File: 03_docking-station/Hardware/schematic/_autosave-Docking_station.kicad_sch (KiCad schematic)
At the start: 22 parts, among them J3 -, J4 +, J5 Conn_01x01, J6 Conn_01x01, J9 Conn_01x02, K1 FINDER-32.21-x000, K2 Relpol, K3 FINDER-32.21-x000, Q1 BC337, U4 LM393

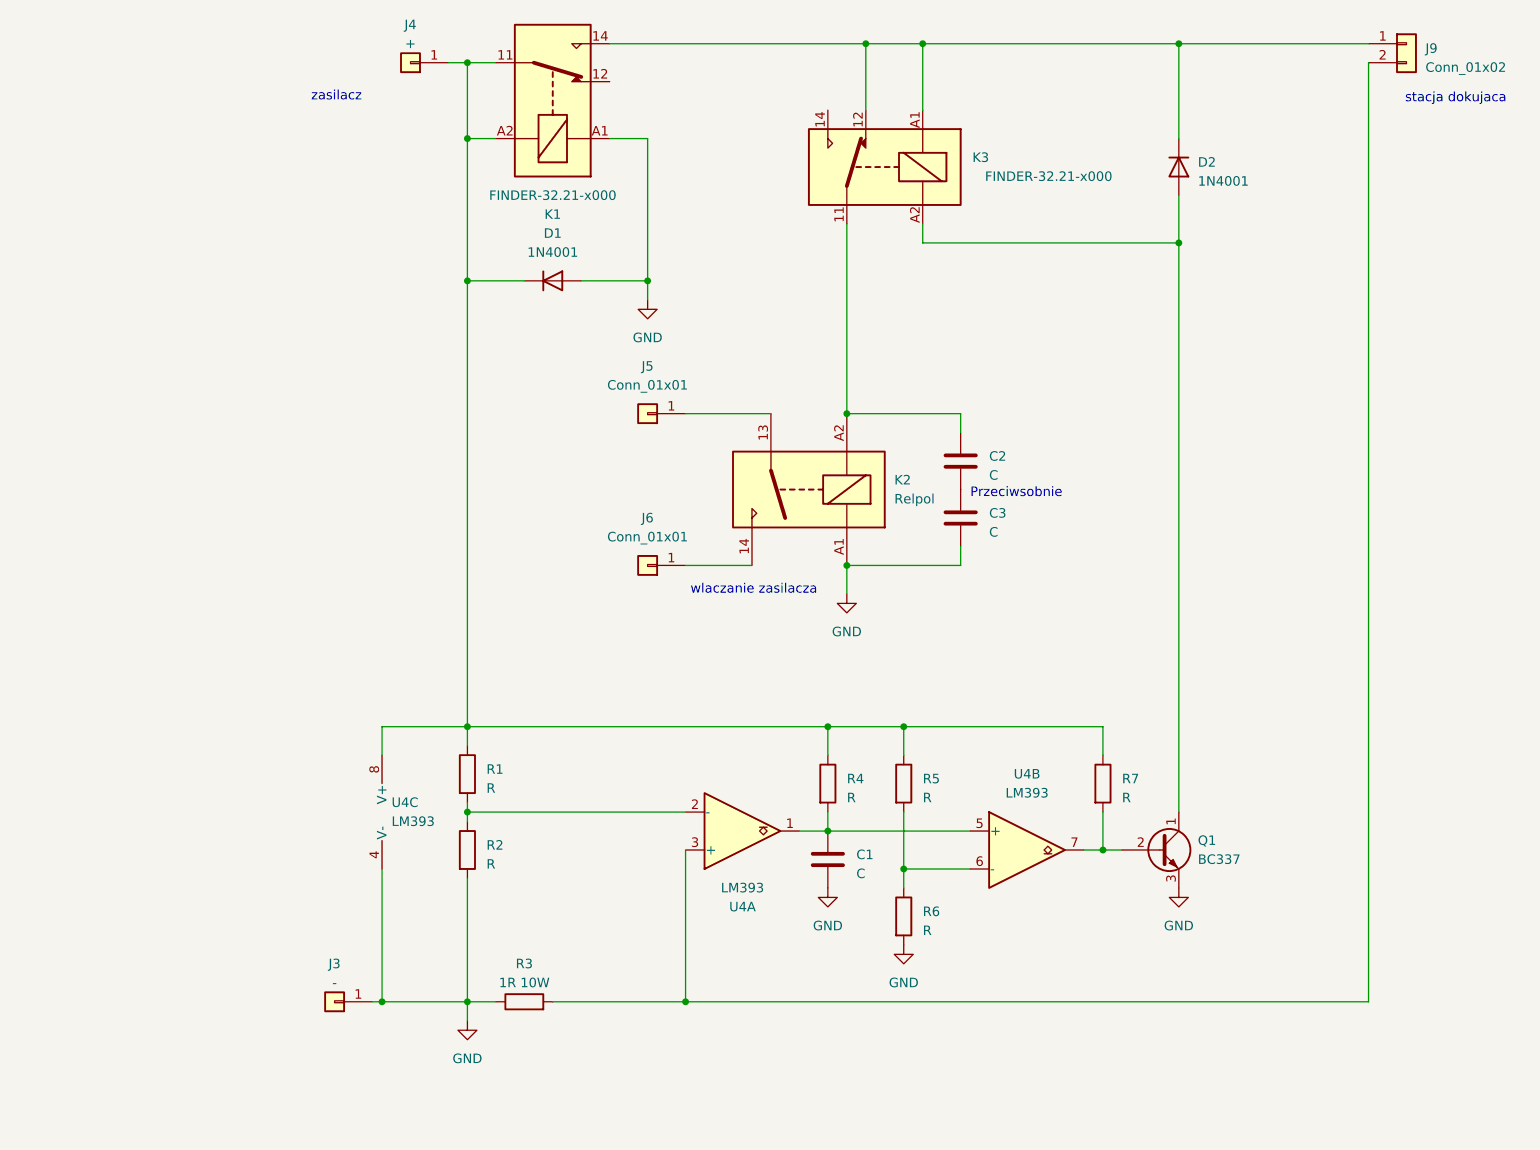
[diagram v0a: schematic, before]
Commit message: minor mistakes fixed; reflected hardware updates
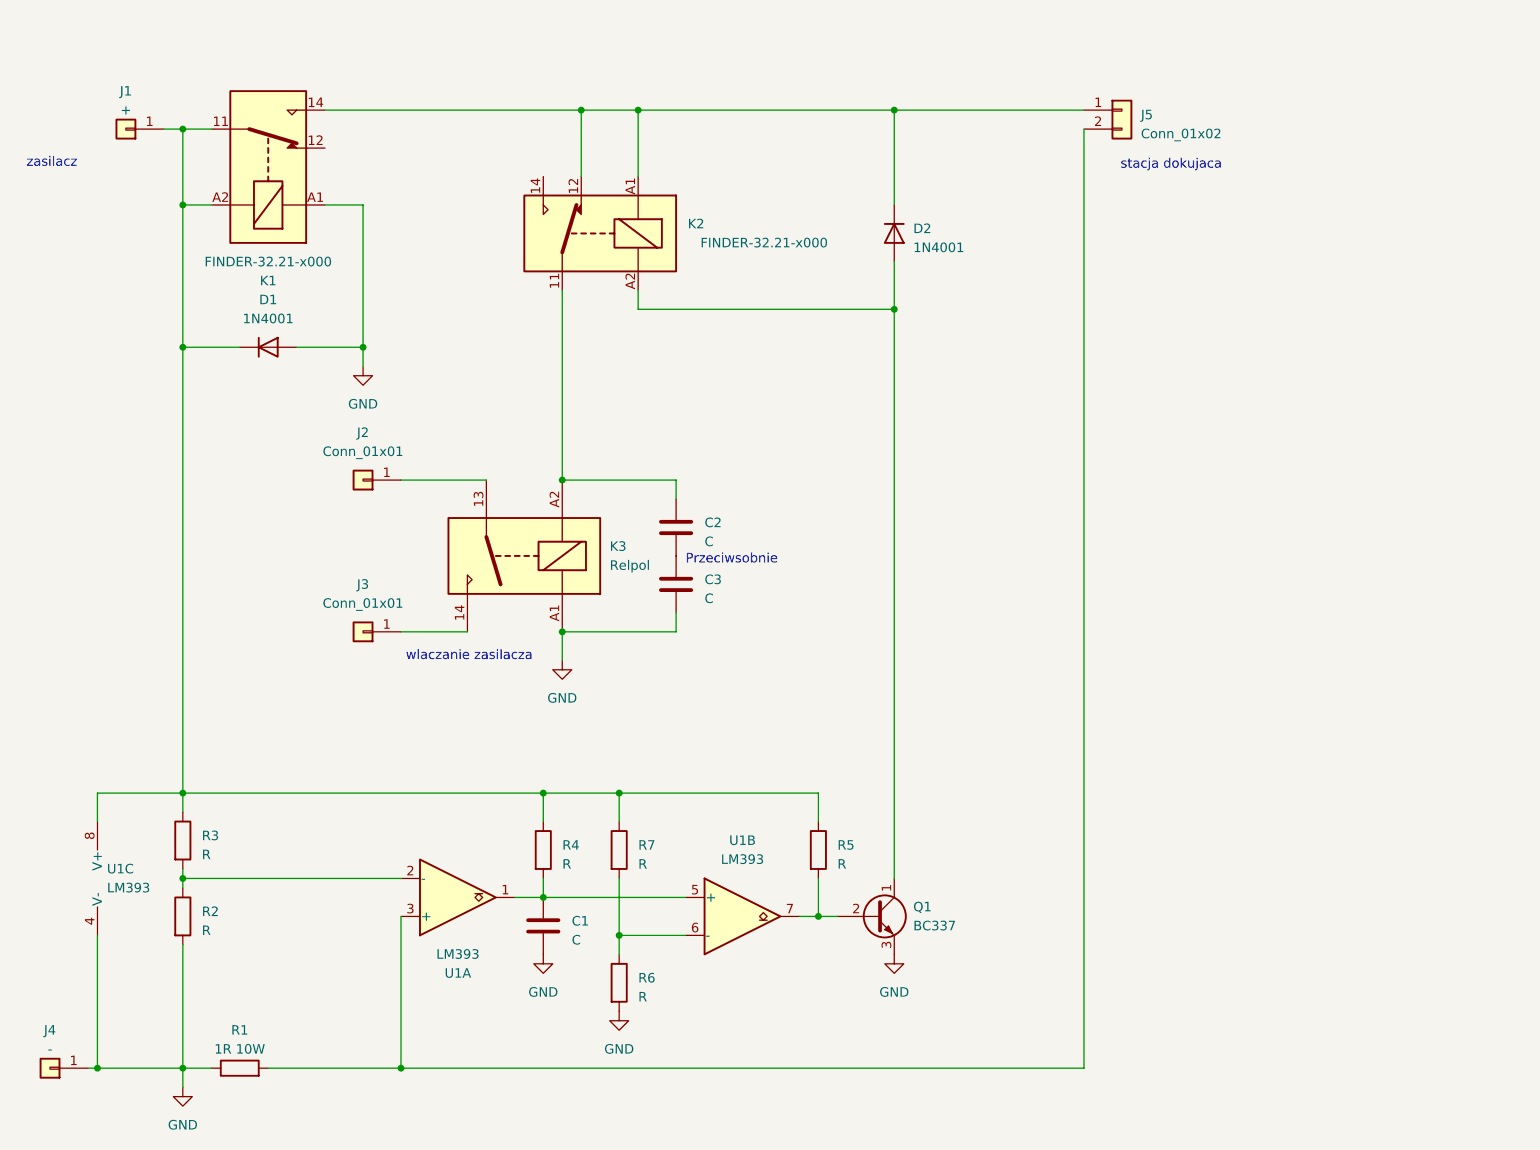
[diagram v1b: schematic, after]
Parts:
- removed J5, J6: Conn_01x01, Connector_Wire:SolderWire-1.5sqmm_1x01_D1.7mm_OD3.9mm, symbol Connector_Generic:Conn_01x01
- removed J9: Conn_01x02, Docking_station:Phoenix, symbol Connector_Generic:Conn_01x02
- removed K2: Relpol, Relay_THT:Relay_SPST_RAYEX-L90AS, symbol Relay:RAYEX-L90AS
- removed K3: FINDER-32.21-x000, Relay_THT:Relay_SPDT_Finder_36.11, symbol Relay:FINDER-32.21-x000
- removed U4: LM393, Package_DIP:DIP-8_W7.62mm_Socket, symbol Comparator:LM393
- added J1: +, Connector_Wire:SolderWire-1.5sqmm_1x01_D1.7mm_OD3.9mm, symbol Connector_Generic:Conn_01x01
- added J2: Conn_01x01, Connector_Wire:SolderWire-1.5sqmm_1x01_D1.7mm_OD3.9mm, symbol Connector_Generic:Conn_01x01
- added J5: Conn_01x02, Docking_station:Phoenix, symbol Connector_Generic:Conn_01x02
- added K2: FINDER-32.21-x000, Relay_THT:Relay_SPDT_Finder_36.11, symbol Relay:FINDER-32.21-x000
- added K3: Relpol, Relay_THT:Relay_SPST_RAYEX-L90AS, symbol Relay:RAYEX-L90AS
- added U1: LM393, Package_DIP:DIP-8_W7.62mm_Socket, symbol Comparator:LM393
- J3: value - -> Conn_01x01
- J4: value + -> -
- R1: value R -> 1R 10W; footprint Resistor_THT:R_Axial_DIN0207_L6.3mm_D2.5mm_P7.62mm_Horizontal -> Resistor_THT:R_Axial_Power_L50.0mm_W9.0mm_P60.96mm
- R3: value 1R 10W -> R; footprint Resistor_THT:R_Axial_Power_L50.0mm_W9.0mm_P60.96mm -> Resistor_THT:R_Axial_DIN0207_L6.3mm_D2.5mm_P7.62mm_Horizontal
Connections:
- net GND: now also J4.1 (Pin_1), R1.1, K3.A1, U1.4 (V-); no longer J3.1 (Pin_1), R3.1
- net at D2.1 (K), K1.14: now also J5.1 (Pin_1), K2.12, K2.A1
- net at R3.2: now also R2.1, U1.2 (-)
- net at D1.1 (K), K1.11, K1.A2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: now also R3.1, J1.1 (Pin_1), U1.8 (V+); no longer J4.1 (Pin_1), R1.1
- net at R1.2: now also J5.2 (Pin_2), U1.3 (+); no longer R2.1
- net at C1.1, R4.2: now also U1.1, U1.5 (+)
- net at R7.2: now also R6.1, U1.6 (-); no longer Q1.2 (B)
- net at D2.2 (A), Q1.1 (C): now also K2.A2
- net at R5.2: now also Q1.2 (B), U1.7; no longer R6.1
- net at C2.1: now also K2.11, K3.A2
- new net: J2.1 (Pin_1), K3.13
- new net: J3.1 (Pin_1), K3.14
